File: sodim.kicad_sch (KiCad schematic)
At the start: 10 parts

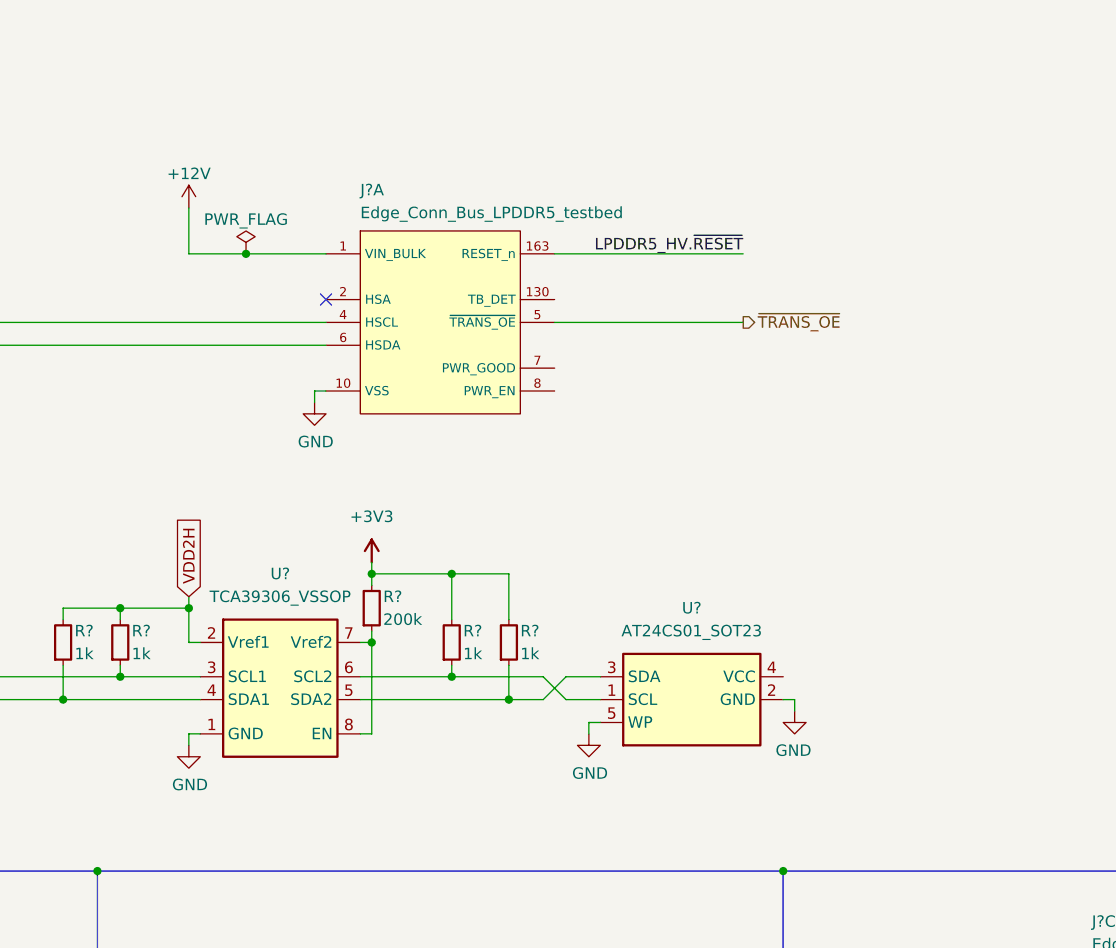
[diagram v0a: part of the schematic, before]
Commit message: [#52835] schematics: add I2C line, VIN_BULK is 5V
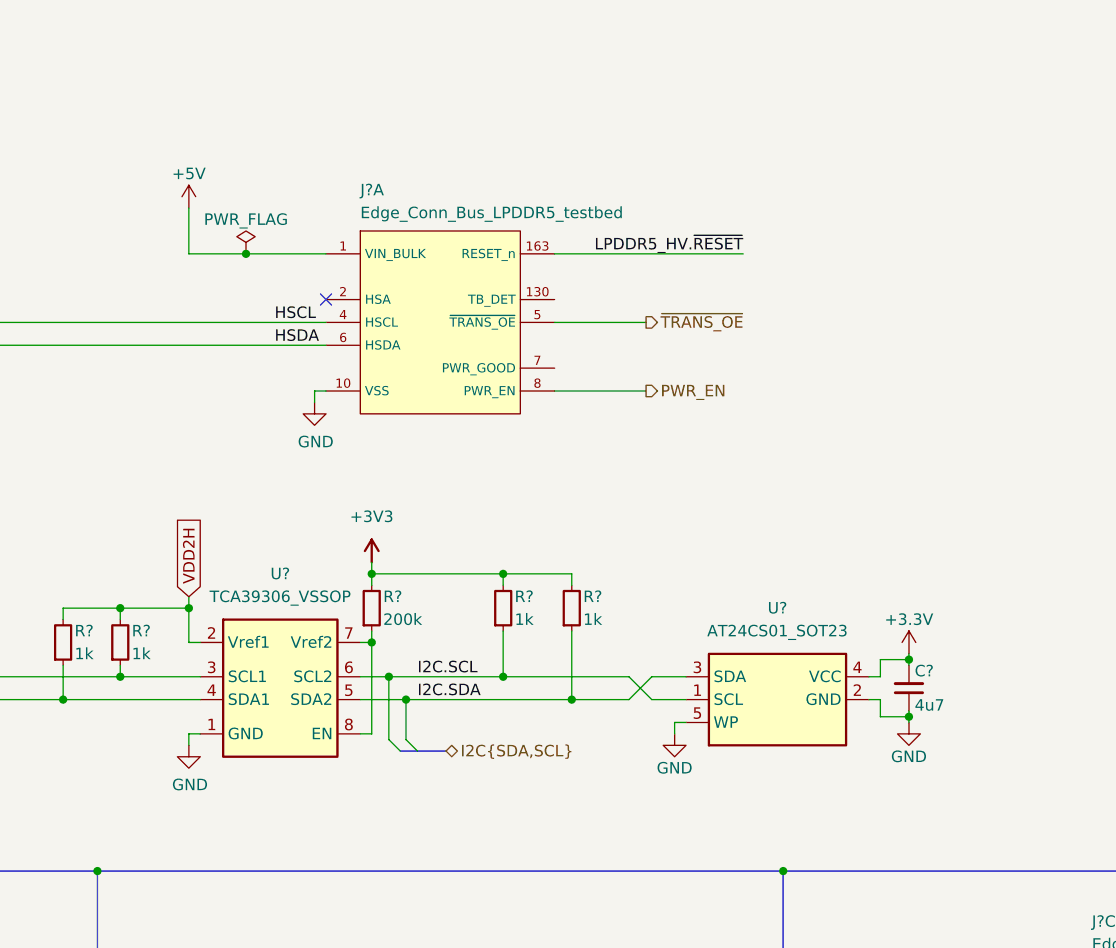
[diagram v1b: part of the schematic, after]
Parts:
- added C?: C_4u7_0402, antmicro-footprints:C_0402_1005Metric, symbol antmicroCapacitors0402:C_4u7_0402
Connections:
- net +3V3: now also U?.4 (VCC), C?.2
- net GND: now also C?.1
- net I2C.SCL: now reaches R?.1, U?.1 (SCL), U?.6 (SCL2)
- net HSCL: now reaches J?.4 (HSCL), R?.1, U?.3 (SCL1)
- net HSDA: now reaches J?.6 (HSDA), R?.1, U?.4 (SDA1)
- net I2C.SDA: now reaches R?.1, U?.3 (SDA), U?.5 (SDA2)
- net PWR_EN: now reaches J?.8 (PWR_EN)
- net +12V renamed +5V
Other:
- moved on the sheet: R?, U?

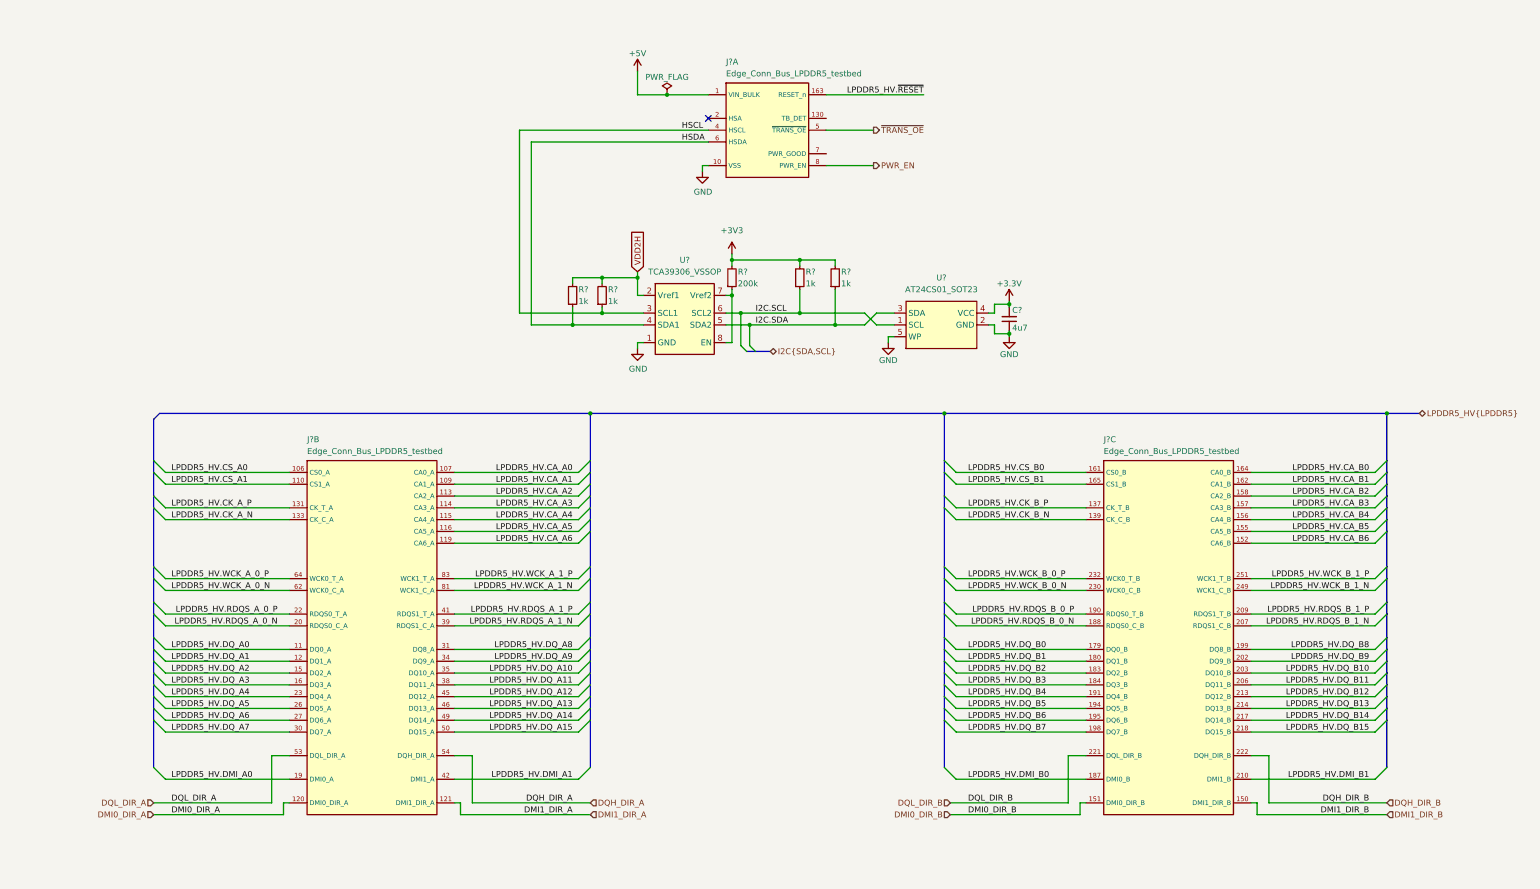
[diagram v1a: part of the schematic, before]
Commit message: [#52835] schematics: update LPDDR5 connections, finish translators subsheet
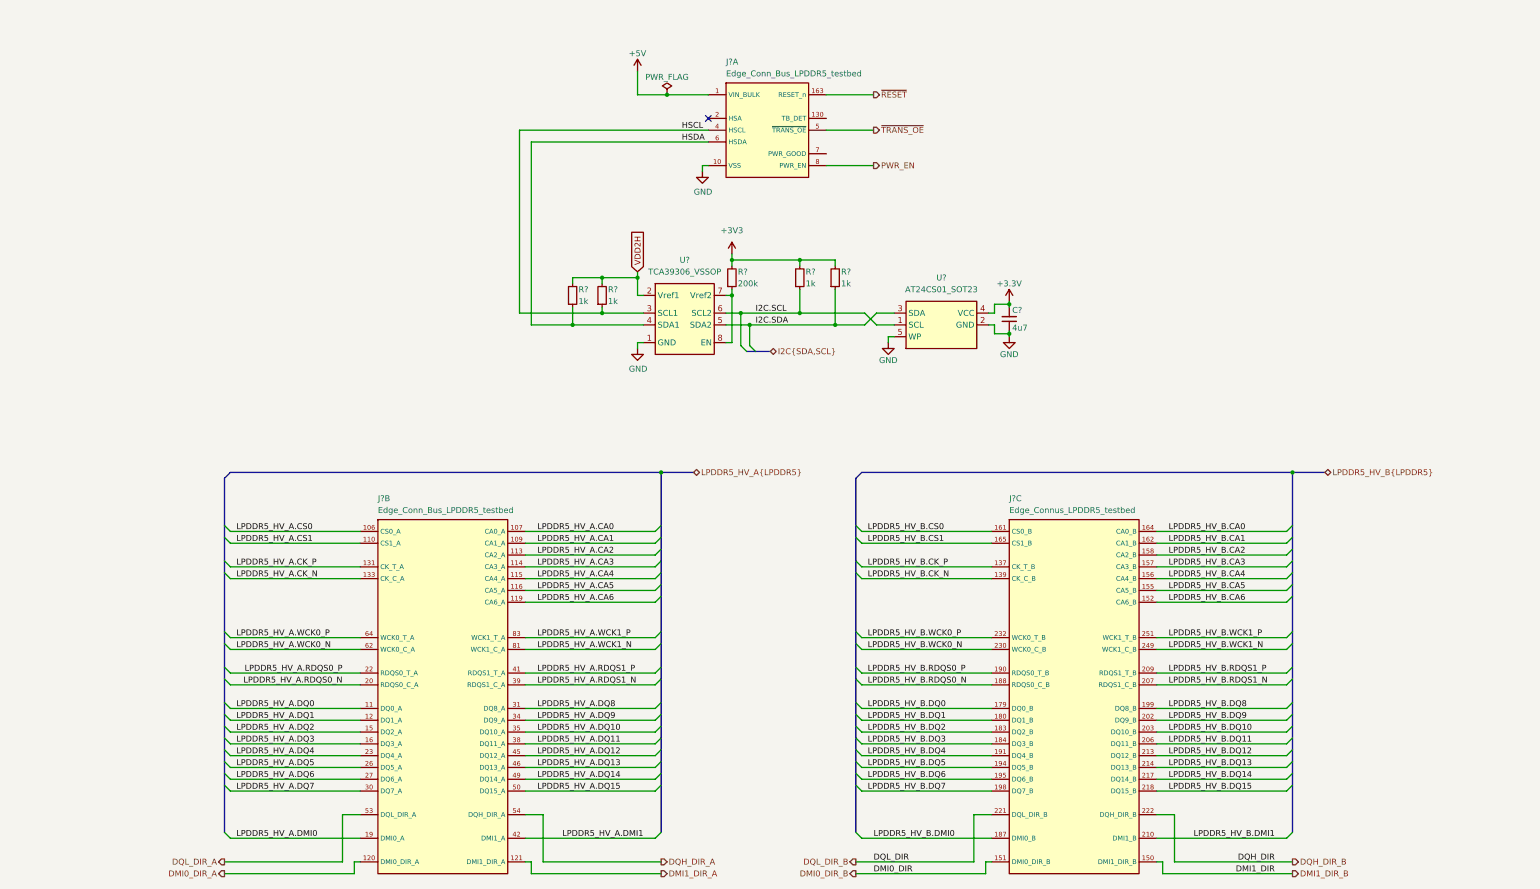
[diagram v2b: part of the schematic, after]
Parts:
- removed J? (x2): Edge_Conn_Bus_LPDDR5_testbed, antmicro-footprints:Edge_Conn_Bus_DDR5_SODIMM, symbol antmicroMemoryConnectorsPCCardSockets:Edge_Conn_Bus_LPDDR5_testbed
- added J?: Edge_Connus_LPDDR5_testbed, antmicro-footprints:Edge_Conn_Bus_DDR5_SODIMM, symbol antmicroMemoryConnectorsPCCardSockets:Edge_Conn_Bus_LPDDR5_testbed
- added J?: Edge_Conn_Bus_LPDDR5_testbed, antmicro-footprints:Edge_Conn_Bus_DDR5_SODIMM, symbol antmicroMemoryConnectorsPCCardSockets:Edge_Conn_Bus_LPDDR5_testbed
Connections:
- net DMI0_DIR_A: now also J?.120 (DMI0_DIR_A)
- net DMI0_DIR_B: now also J?.151 (DMI0_DIR_B)
- net DMI1_DIR_A: now also J?.121 (DMI1_DIR_A)
- net DMI1_DIR_B: now also J?.150 (DMI1_DIR_B)
- net DQH_DIR_A: now also J?.54 (DQH_DIR_A)
- net DQH_DIR_B: now also J?.222 (DQH_DIR_B)
- net DQL_DIR_A: now also J?.53 (DQL_DIR_A)
- net DQL_DIR_B: now also J?.221 (DQL_DIR_B)
- net LPDDR5_HV.~{RESET} renamed ~{RESET}
- new net LPDDR5_HV_A.CA0: J?.107 (CA0_A)
- new net LPDDR5_HV_A.CA1: J?.109 (CA1_A)
- new net LPDDR5_HV_A.CA2: J?.113 (CA2_A)
- new net LPDDR5_HV_A.CA3: J?.114 (CA3_A)
- new net LPDDR5_HV_A.CA4: J?.115 (CA4_A)
- new net LPDDR5_HV_A.CA5: J?.116 (CA5_A)
- new net LPDDR5_HV_A.CA6: J?.119 (CA6_A)
- new net LPDDR5_HV_A.CK_N: J?.133 (CK_C_A)
- new net LPDDR5_HV_A.CK_P: J?.131 (CK_T_A)
- new net LPDDR5_HV_A.CS0: J?.106 (CS0_A)
- new net LPDDR5_HV_A.CS1: J?.110 (CS1_A)
- new net LPDDR5_HV_A.DMI0: J?.19 (DMI0_A)
- new net LPDDR5_HV_A.DMI1: J?.42 (DMI1_A)
- new net LPDDR5_HV_A.DQ0: J?.11 (DQ0_A)
- new net LPDDR5_HV_A.DQ1: J?.12 (DQ1_A)
- new net LPDDR5_HV_A.DQ10: J?.35 (DQ10_A)
- new net LPDDR5_HV_A.DQ11: J?.38 (DQ11_A)
- new net LPDDR5_HV_A.DQ12: J?.45 (DQ12_A)
- new net LPDDR5_HV_A.DQ13: J?.46 (DQ13_A)
- new net LPDDR5_HV_A.DQ14: J?.49 (DQ14_A)
- new net LPDDR5_HV_A.DQ15: J?.50 (DQ15_A)
- new net LPDDR5_HV_A.DQ2: J?.15 (DQ2_A)
- new net LPDDR5_HV_A.DQ3: J?.16 (DQ3_A)
- new net LPDDR5_HV_A.DQ4: J?.23 (DQ4_A)
- new net LPDDR5_HV_A.DQ5: J?.26 (DQ5_A)
- new net LPDDR5_HV_A.DQ6: J?.27 (DQ6_A)
- new net LPDDR5_HV_A.DQ7: J?.30 (DQ7_A)
- new net LPDDR5_HV_A.DQ8: J?.31 (DQ8_A)
- new net LPDDR5_HV_A.DQ9: J?.34 (DQ9_A)
- new net LPDDR5_HV_A.RDQS0_N: J?.20 (RDQS0_C_A)
- new net LPDDR5_HV_A.RDQS0_P: J?.22 (RDQS0_T_A)
- new net LPDDR5_HV_A.RDQS1_N: J?.39 (RDQS1_C_A)
- new net LPDDR5_HV_A.RDQS1_P: J?.41 (RDQS1_T_A)
- new net LPDDR5_HV_A.WCK0_N: J?.62 (WCK0_C_A)
- new net LPDDR5_HV_A.WCK0_P: J?.64 (WCK0_T_A)
- new net LPDDR5_HV_A.WCK1_N: J?.81 (WCK1_C_A)
- new net LPDDR5_HV_A.WCK1_P: J?.83 (WCK1_T_A)
- new net LPDDR5_HV_B.CA0: J?.164 (CA0_B)
- new net LPDDR5_HV_B.CA1: J?.162 (CA1_B)
- new net LPDDR5_HV_B.CA2: J?.158 (CA2_B)
- new net LPDDR5_HV_B.CA3: J?.157 (CA3_B)
- new net LPDDR5_HV_B.CA4: J?.156 (CA4_B)
- new net LPDDR5_HV_B.CA5: J?.155 (CA5_B)
- new net LPDDR5_HV_B.CA6: J?.152 (CA6_B)
- new net LPDDR5_HV_B.CK_N: J?.139 (CK_C_B)
- new net LPDDR5_HV_B.CK_P: J?.137 (CK_T_B)
- new net LPDDR5_HV_B.CS0: J?.161 (CS0_B)
- new net LPDDR5_HV_B.CS1: J?.165 (CS1_B)
- new net LPDDR5_HV_B.DMI0: J?.187 (DMI0_B)
- new net LPDDR5_HV_B.DMI1: J?.210 (DMI1_B)
- new net LPDDR5_HV_B.DQ0: J?.179 (DQ0_B)
- new net LPDDR5_HV_B.DQ1: J?.180 (DQ1_B)
- new net LPDDR5_HV_B.DQ10: J?.203 (DQ10_B)
- new net LPDDR5_HV_B.DQ11: J?.206 (DQ11_B)
- new net LPDDR5_HV_B.DQ12: J?.213 (DQ12_B)
- new net LPDDR5_HV_B.DQ13: J?.214 (DQ13_B)
- new net LPDDR5_HV_B.DQ14: J?.217 (DQ14_B)
- new net LPDDR5_HV_B.DQ15: J?.218 (DQ15_B)
- new net LPDDR5_HV_B.DQ2: J?.183 (DQ2_B)
- new net LPDDR5_HV_B.DQ3: J?.184 (DQ3_B)
- new net LPDDR5_HV_B.DQ4: J?.191 (DQ4_B)
- new net LPDDR5_HV_B.DQ5: J?.194 (DQ5_B)
- new net LPDDR5_HV_B.DQ6: J?.195 (DQ6_B)
- new net LPDDR5_HV_B.DQ7: J?.198 (DQ7_B)
- new net LPDDR5_HV_B.DQ8: J?.199 (DQ8_B)
- new net LPDDR5_HV_B.DQ9: J?.202 (DQ9_B)
- new net LPDDR5_HV_B.RDQS0_N: J?.188 (RDQS0_C_B)
- new net LPDDR5_HV_B.RDQS0_P: J?.190 (RDQS0_T_B)
- new net LPDDR5_HV_B.RDQS1_N: J?.207 (RDQS1_C_B)
- new net LPDDR5_HV_B.RDQS1_P: J?.209 (RDQS1_T_B)
- new net LPDDR5_HV_B.WCK0_N: J?.230 (WCK0_C_B)
- new net LPDDR5_HV_B.WCK0_P: J?.232 (WCK0_T_B)
- new net LPDDR5_HV_B.WCK1_N: J?.249 (WCK1_C_B)
- new net LPDDR5_HV_B.WCK1_P: J?.251 (WCK1_T_B)

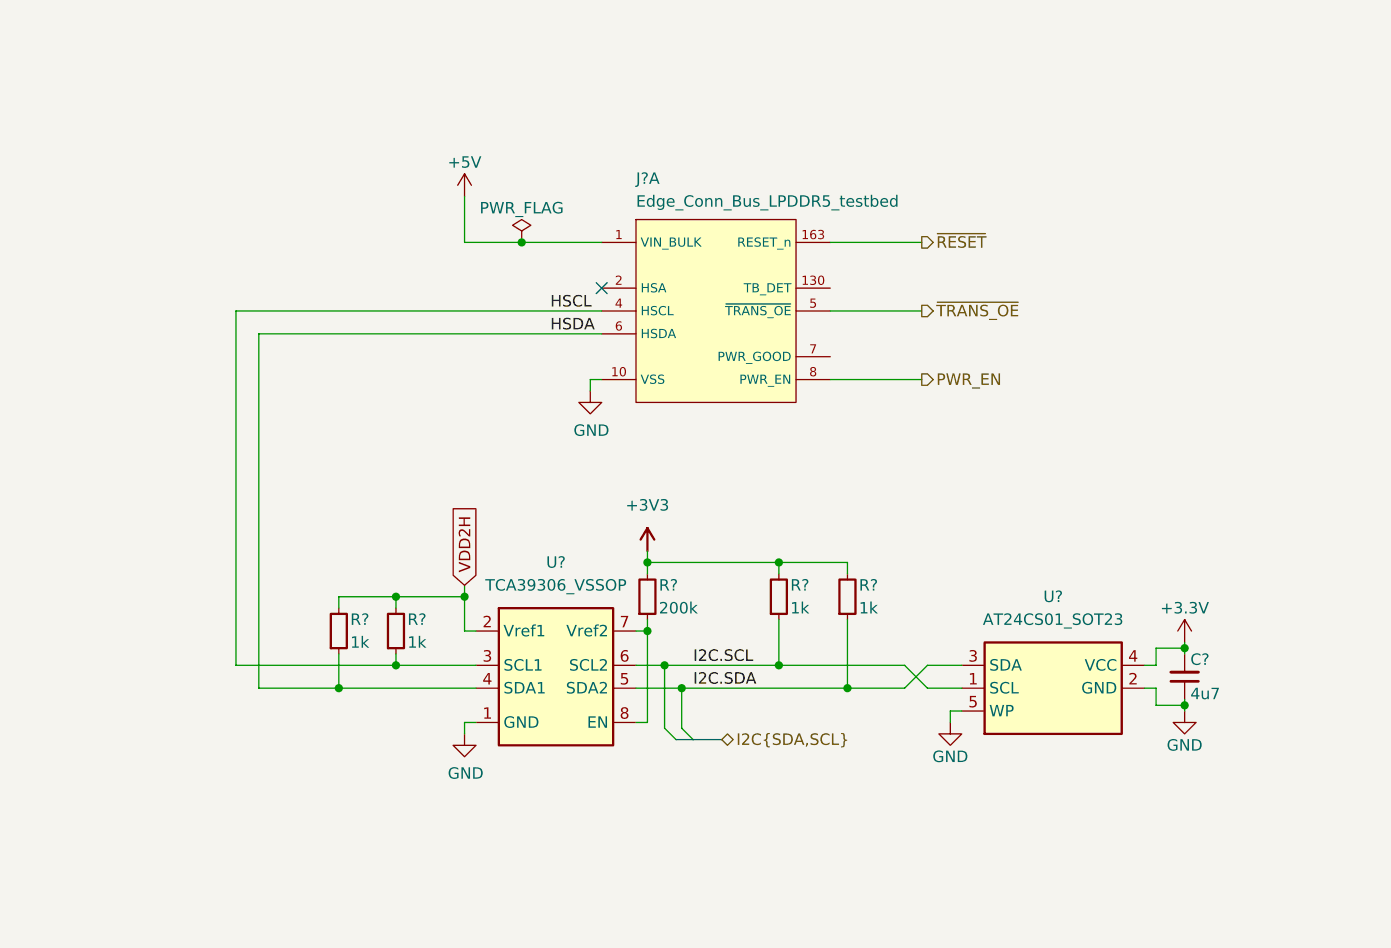
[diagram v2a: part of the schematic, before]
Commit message: [#52536] schematics: setup resistor dividers for DCDC converter
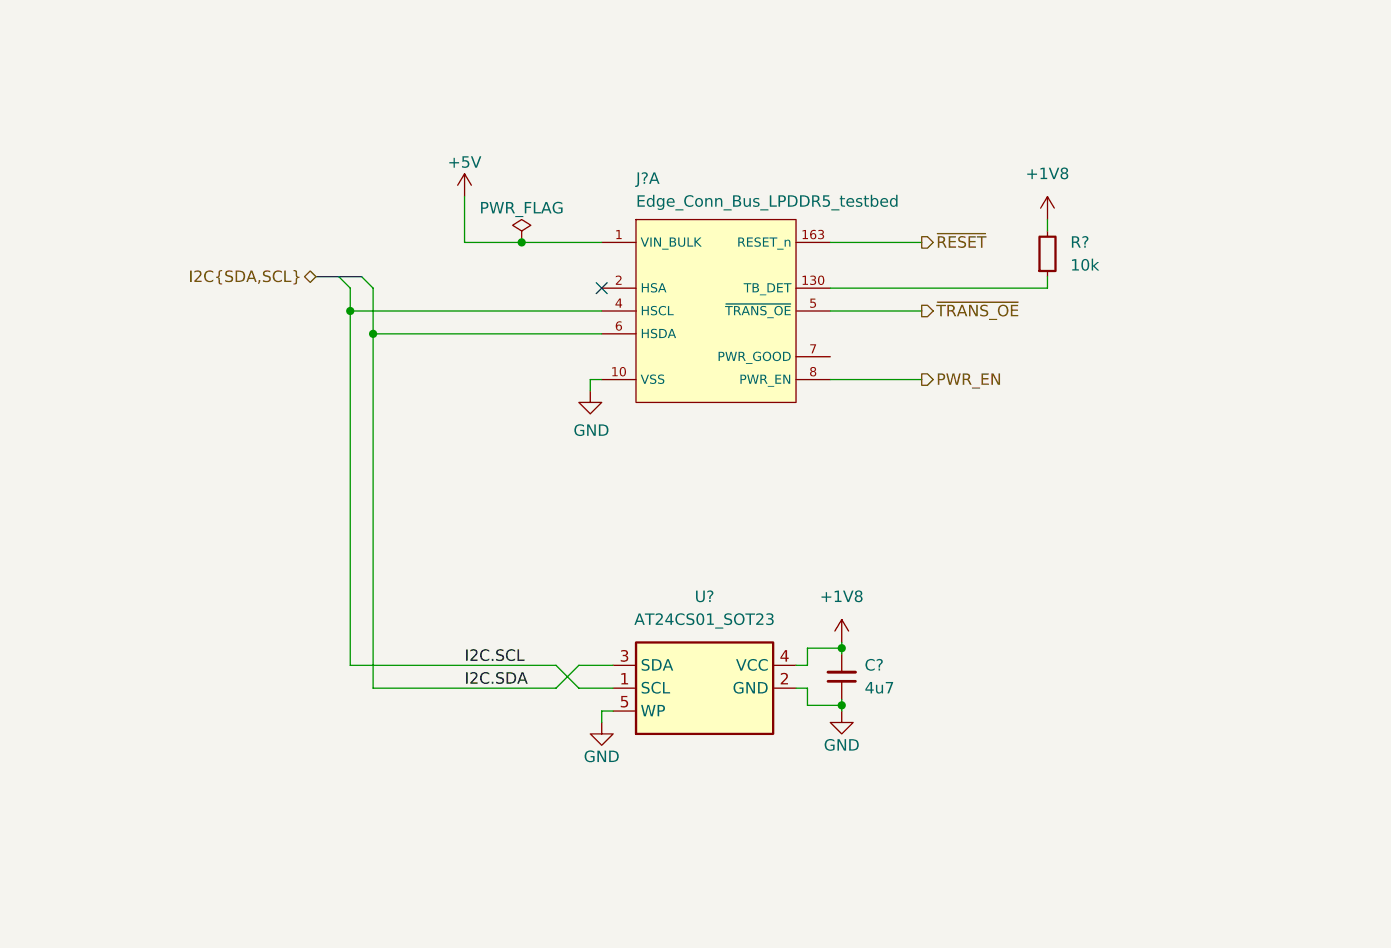
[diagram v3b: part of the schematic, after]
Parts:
- removed C?: C_4u7_0402, antmicro-footprints:C_0402_1005Metric, symbol antmicroCapacitors0402:C_4u7_0402
- removed R? (x4): R_1k_0402, antmicro-footprints:R_0402_1005Metric, symbol antmicroResistors0402:R_1k_0402
- removed R?: R_200k_0402, antmicro-footprints:R_0402_1005Metric, symbol antmicroResistors0402:R_200k_0402
- removed U?: TCA39306_VSSOP, antmicro-footprints:VSSOP-8_2.3x2mm_P0.5mm, symbol antmicroLogicTranslatorsLevelShifters:TCA39306_VSSOP
- added C?: C_4u7_0402, antmicro-footprints:C_0402_1005Metric, symbol antmicroCapacitors0402:C_4u7_0402
- added R?: R_10k_0402, antmicro-footprints:R_0402_1005Metric, symbol antmicroResistors0402:R_10k_0402
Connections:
- net HSCL is gone; now on net I2C.SCL: J?.4 (HSCL)
- net HSDA is gone; now on net I2C.SDA: J?.6 (HSDA)
- net GND: now also C?.1
- net at J?.130 (TB_DET): now also R?.1
- net +3V3 renamed +1V8
- net +1V8: now also C?.2, R?.2
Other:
- moved on the sheet: U?
